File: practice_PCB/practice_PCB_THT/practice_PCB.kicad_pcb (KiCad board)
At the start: 2 copper layers, 97.5 x 96.5 mm, 224 parts, among them J1 5V, J10 GND, J11 5V, J12 GND, J13 5V, J14 GND, J15 5V, J16 GND, J17 5V, J18 GND, J19 5V, J2 GND, J20 GND, J21 5V, J22 GND, J23 5V, J24 GND, J25 5V, J26 GND, J27 5V, J28 GND, J29 5V, J3 5V, J30 GND, J31 5V, J32 GND, J4 GND, J5 5V, J6 GND, J7 5V, J8 GND, J9 5V

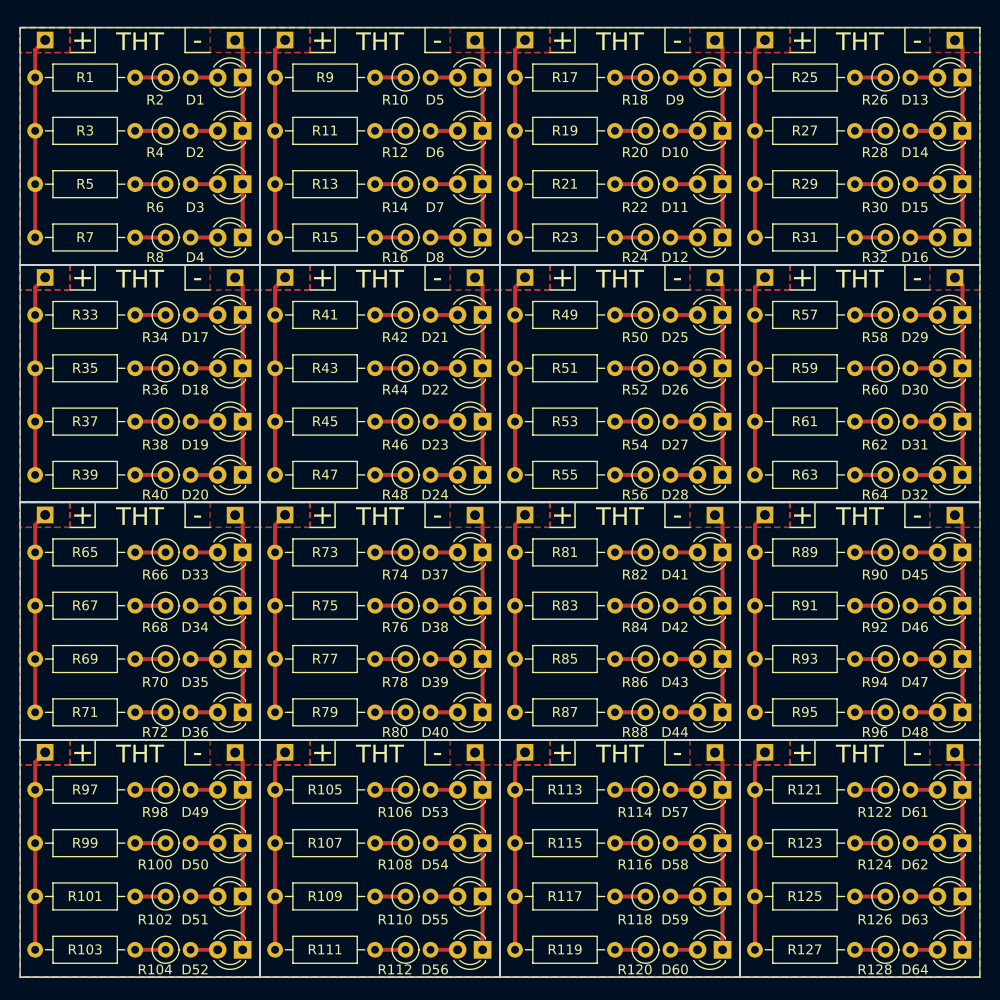
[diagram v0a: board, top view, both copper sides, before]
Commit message: create an array and copy the SMT Array in to the file
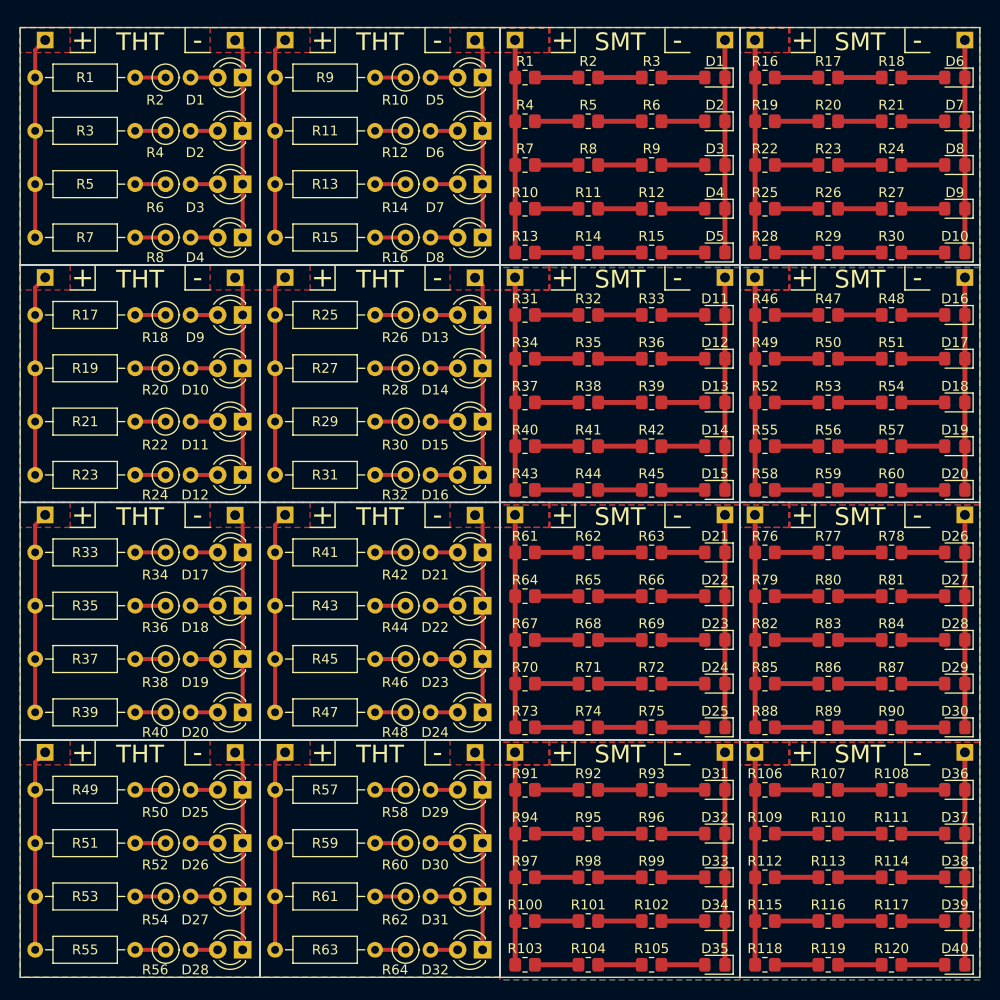
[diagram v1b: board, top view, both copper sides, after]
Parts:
- removed the D10 at (208.5, 76.5)
- removed the D11 at (208.5, 82.0)
- removed the D12 at (208.5, 87.4)
- removed the D13 at (232.9, 71.1)
- removed the D14 at (232.9, 76.5)
- removed the D15 at (232.9, 82.0)
- removed the D16 at (232.9, 87.4)
- removed the D17 at (159.8, 95.2)
- removed the D18 at (159.8, 100.7)
- removed the D19 at (159.8, 106.1)
- removed the D20 at (159.8, 111.5)
- removed the D21 at (184.2, 95.2)
- removed the D22 at (184.2, 100.7)
- removed the D23 at (184.2, 106.1)
- removed the D24 at (184.2, 111.5)
- removed the D25 at (208.5, 95.2)
- removed the D26 at (208.5, 100.7)
- removed the D27 at (208.5, 106.1)
- removed the D28 at (208.5, 111.5)
- removed the D29 at (232.9, 95.2)
- removed the D30 at (232.9, 100.7)
- removed the D31 at (232.9, 106.1)
- removed the D32 at (232.9, 111.5)
- removed D41, D42, D43, D44, D45, D46, D47, D48, D49, D50, D51, D52, D53, D54, D55, D56, D57, D58, D59, D60, D61, D62, D63, D64: LED, LED_THT:LED_D3.0mm
- removed the D9 at (208.5, 71.1)
- removed the J10 at (159.0, 91.5)
- removed the J11 at (164.1, 91.4)
- removed the J12 at (183.4, 91.5)
- removed the J13 at (188.5, 91.4)
- removed the J14 at (207.8, 91.5)
- removed the J15 at (212.9, 91.4)
- removed the J16 at (232.2, 91.5)
- removed J17, J19, J21, J23, J25, J27, J29, J31: 5V, practice_PCB:PinSocket_1x01_P2.54mm_Vertical
- removed J18, J20, J22, J24, J26, J28, J30, J32: GND, practice_PCB:PinSocket_1x01_P2.54mm_Vertical
- removed the J5 at (188.5, 67.3)
- removed the J6 at (207.8, 67.3)
- removed the J7 at (212.9, 67.3)
- removed the J8 at (232.2, 67.3)
- removed the J9 at (139.7, 91.4)
- removed R121, R123, R125, R127: 60, Resistor_THT:R_Axial_DIN0207_L6.3mm_D2.5mm_P10.16mm_Horizontal
- removed R122, R124, R126, R128: 60, Resistor_THT:R_Axial_DIN0207_L6.3mm_D2.5mm_P2.54mm_Vertical
- removed the R17 at (187.5, 71.1)
- removed the R18 at (200.7, 71.1)
- removed the R19 at (187.5, 76.5)
- removed the R20 at (200.7, 76.5)
- removed the R21 at (187.5, 82.0)
- removed the R22 at (200.7, 82.0)
- removed the R23 at (187.5, 87.4)
- removed the R24 at (200.7, 87.4)
- removed the R25 at (211.8, 71.1)
- removed the R26 at (225.1, 71.1)
- removed the R27 at (211.8, 76.5)
- removed the R28 at (225.1, 76.5)
- removed the R29 at (211.8, 82.0)
- removed the R30 at (225.1, 82.0)
- removed the R31 at (211.8, 87.4)
- removed the R32 at (225.1, 87.4)
- removed the R33 at (138.7, 95.2)
- removed the R34 at (151.9, 95.2)
- removed the R35 at (138.7, 100.7)
- removed the R36 at (151.9, 100.7)
- removed the R37 at (138.7, 106.1)
- removed the R38 at (151.9, 106.1)
- removed the R39 at (138.7, 111.5)
- removed the R40 at (151.9, 111.5)
- removed the R41 at (163.1, 95.2)
- removed the R42 at (176.3, 95.2)
- removed the R43 at (163.1, 100.7)
- removed the R44 at (176.3, 100.7)
- removed the R45 at (163.1, 106.1)
- removed the R46 at (176.3, 106.1)
- removed the R47 at (163.1, 111.5)
- removed the R48 at (176.3, 111.5)
- removed the R49 at (187.5, 95.2)
- removed the R50 at (200.7, 95.2)
- removed the R51 at (187.5, 100.7)
- removed the R52 at (200.7, 100.7)
- removed the R53 at (187.5, 106.1)
- removed the R54 at (200.7, 106.1)
- removed the R55 at (187.5, 111.5)
- removed the R56 at (200.7, 111.5)
- removed the R57 at (211.8, 95.2)
- removed the R58 at (225.1, 95.2)
- removed the R59 at (211.8, 100.7)
- removed the R60 at (225.1, 100.7)
- removed the R61 at (211.8, 106.1)
- removed the R62 at (225.1, 106.1)
- removed the R63 at (211.8, 111.5)
- removed the R64 at (225.1, 111.5)
- added D1: LED, LED_SMD:LED_0805_2012Metric_Pad1.15x1.40mm_HandSolder, F.Cu at (207.8, 71.1)
- added D10: LED, LED_SMD:LED_0805_2012Metric_Pad1.15x1.40mm_HandSolder, F.Cu at (232.1, 88.9)
- added D10: LED, LED_THT:LED_D3.0mm, F.Cu at (159.8, 100.7)
- added D11: LED, LED_THT:LED_D3.0mm, F.Cu at (159.8, 106.1)
- added D11: LED, LED_SMD:LED_0805_2012Metric_Pad1.15x1.40mm_HandSolder, F.Cu at (207.8, 95.2)
- added D12: LED, LED_SMD:LED_0805_2012Metric_Pad1.15x1.40mm_HandSolder, F.Cu at (207.8, 99.7)
- added D12: LED, LED_THT:LED_D3.0mm, F.Cu at (159.8, 111.5)
- added D13: LED, LED_THT:LED_D3.0mm, F.Cu at (184.2, 95.2)
- added D13: LED, LED_SMD:LED_0805_2012Metric_Pad1.15x1.40mm_HandSolder, F.Cu at (207.8, 104.1)
- added D14: LED, LED_SMD:LED_0805_2012Metric_Pad1.15x1.40mm_HandSolder, F.Cu at (207.8, 108.6)
- added D14: LED, LED_THT:LED_D3.0mm, F.Cu at (184.2, 100.7)
- added D15: LED, LED_THT:LED_D3.0mm, F.Cu at (184.2, 106.1)
- added D15: LED, LED_SMD:LED_0805_2012Metric_Pad1.15x1.40mm_HandSolder, F.Cu at (207.8, 113.0)
- added D16: LED, LED_THT:LED_D3.0mm, F.Cu at (184.2, 111.5)
- added D16: LED, LED_SMD:LED_0805_2012Metric_Pad1.15x1.40mm_HandSolder, F.Cu at (232.1, 95.2)
- added D17: LED, LED_THT:LED_D3.0mm, F.Cu at (159.8, 119.4)
- added D17: LED, LED_SMD:LED_0805_2012Metric_Pad1.15x1.40mm_HandSolder, F.Cu at (232.1, 99.7)
- added D18: LED, LED_SMD:LED_0805_2012Metric_Pad1.15x1.40mm_HandSolder, F.Cu at (232.1, 104.1)
- added D18: LED, LED_THT:LED_D3.0mm, F.Cu at (159.8, 124.8)
- added D19: LED, LED_THT:LED_D3.0mm, F.Cu at (159.8, 130.2)
- added D19: LED, LED_SMD:LED_0805_2012Metric_Pad1.15x1.40mm_HandSolder, F.Cu at (232.1, 108.6)
- added D2: LED, LED_SMD:LED_0805_2012Metric_Pad1.15x1.40mm_HandSolder, F.Cu at (207.8, 75.6)
- added D20: LED, LED_SMD:LED_0805_2012Metric_Pad1.15x1.40mm_HandSolder, F.Cu at (232.1, 113.0)
- added D20: LED, LED_THT:LED_D3.0mm, F.Cu at (159.8, 135.6)
- added D21: LED, LED_THT:LED_D3.0mm, F.Cu at (184.2, 119.4)
- added D21: LED, LED_SMD:LED_0805_2012Metric_Pad1.15x1.40mm_HandSolder, F.Cu at (207.8, 119.4)
- added D22: LED, LED_THT:LED_D3.0mm, F.Cu at (184.2, 124.8)
- added D22: LED, LED_SMD:LED_0805_2012Metric_Pad1.15x1.40mm_HandSolder, F.Cu at (207.8, 123.8)
- added D23: LED, LED_SMD:LED_0805_2012Metric_Pad1.15x1.40mm_HandSolder, F.Cu at (207.8, 128.3)
- added D23: LED, LED_THT:LED_D3.0mm, F.Cu at (184.2, 130.2)
- added D24: LED, LED_SMD:LED_0805_2012Metric_Pad1.15x1.40mm_HandSolder, F.Cu at (207.8, 132.7)
- added D24: LED, LED_THT:LED_D3.0mm, F.Cu at (184.2, 135.6)
- added D25: LED, LED_SMD:LED_0805_2012Metric_Pad1.15x1.40mm_HandSolder, F.Cu at (207.8, 137.2)
- added D25: LED, LED_THT:LED_D3.0mm, F.Cu at (159.8, 143.5)
- added D26: LED, LED_THT:LED_D3.0mm, F.Cu at (159.8, 148.9)
- added D26: LED, LED_SMD:LED_0805_2012Metric_Pad1.15x1.40mm_HandSolder, F.Cu at (232.1, 119.4)
- added D27: LED, LED_SMD:LED_0805_2012Metric_Pad1.15x1.40mm_HandSolder, F.Cu at (232.1, 123.8)
- added D27: LED, LED_THT:LED_D3.0mm, F.Cu at (159.8, 154.3)
- added D28: LED, LED_SMD:LED_0805_2012Metric_Pad1.15x1.40mm_HandSolder, F.Cu at (232.1, 128.3)
- added D28: LED, LED_THT:LED_D3.0mm, F.Cu at (159.8, 159.8)
- added D29: LED, LED_THT:LED_D3.0mm, F.Cu at (184.2, 143.5)
- added D29: LED, LED_SMD:LED_0805_2012Metric_Pad1.15x1.40mm_HandSolder, F.Cu at (232.1, 132.7)
- added D3: LED, LED_SMD:LED_0805_2012Metric_Pad1.15x1.40mm_HandSolder, F.Cu at (207.8, 80.0)
- added D30: LED, LED_THT:LED_D3.0mm, F.Cu at (184.2, 148.9)
- added D30: LED, LED_SMD:LED_0805_2012Metric_Pad1.15x1.40mm_HandSolder, F.Cu at (232.1, 137.2)
- added D31: LED, LED_SMD:LED_0805_2012Metric_Pad1.15x1.40mm_HandSolder, F.Cu at (207.8, 143.5)
- added D31: LED, LED_THT:LED_D3.0mm, F.Cu at (184.2, 154.3)
- added D32: LED, LED_THT:LED_D3.0mm, F.Cu at (184.2, 159.8)
- added D32: LED, LED_SMD:LED_0805_2012Metric_Pad1.15x1.40mm_HandSolder, F.Cu at (207.8, 148.0)
- added D4: LED, LED_SMD:LED_0805_2012Metric_Pad1.15x1.40mm_HandSolder, F.Cu at (207.8, 84.5)
- added D5: LED, LED_SMD:LED_0805_2012Metric_Pad1.15x1.40mm_HandSolder, F.Cu at (207.8, 88.9)
- added D6: LED, LED_SMD:LED_0805_2012Metric_Pad1.15x1.40mm_HandSolder, F.Cu at (232.1, 71.1)
- added D7: LED, LED_SMD:LED_0805_2012Metric_Pad1.15x1.40mm_HandSolder, F.Cu at (232.1, 75.6)
- added D8: LED, LED_SMD:LED_0805_2012Metric_Pad1.15x1.40mm_HandSolder, F.Cu at (232.1, 80.0)
- added D9: LED, LED_SMD:LED_0805_2012Metric_Pad1.15x1.40mm_HandSolder, F.Cu at (232.1, 84.5)
- added D9: LED, LED_THT:LED_D3.0mm, F.Cu at (159.8, 95.2)
- added G***: LOGO, practice_PCB:MWG, B.Cu at (205.7, 86.4)
- added G***1: LOGO, practice_PCB:MWG, B.Cu at (230.1, 86.4)
- added G***2: LOGO, practice_PCB:MWG, B.Cu at (205.7, 110.5)
- added G***3: LOGO, practice_PCB:MWG, B.Cu at (230.1, 110.5)
- added G***4: LOGO, practice_PCB:MWG, B.Cu at (205.7, 134.6)
- added G***5: LOGO, practice_PCB:MWG, B.Cu at (230.1, 134.6)
- added G***6: LOGO, practice_PCB:MWG, B.Cu at (205.7, 158.8)
- added G***7: LOGO, practice_PCB:MWG, B.Cu at (230.1, 158.8)
- added J1: 5V, practice_PCB:PinSocket_1x01_P2.54mm_Vertical, F.Cu at (187.5, 67.3)
- added J10: GND, practice_PCB:PinSocket_1x01_P2.54mm_Vertical, F.Cu at (159.0, 115.6)
- added J10: GND, practice_PCB:PinSocket_1x01_P2.54mm_Vertical, F.Cu at (208.8, 115.6)
- added J11: 5V, practice_PCB:PinSocket_1x01_P2.54mm_Vertical, F.Cu at (164.1, 115.6)
- added J11: 5V, practice_PCB:PinSocket_1x01_P2.54mm_Vertical, F.Cu at (211.8, 115.6)
- added J12: GND, practice_PCB:PinSocket_1x01_P2.54mm_Vertical, F.Cu at (183.4, 115.6)
- added J12: GND, practice_PCB:PinSocket_1x01_P2.54mm_Vertical, F.Cu at (233.2, 115.6)
- added J13: 5V, practice_PCB:PinSocket_1x01_P2.54mm_Vertical, F.Cu at (139.7, 139.7)
- added J13: 5V, practice_PCB:PinSocket_1x01_P2.54mm_Vertical, F.Cu at (187.5, 139.7)
- added J14: GND, practice_PCB:PinSocket_1x01_P2.54mm_Vertical, F.Cu at (159.0, 139.7)
- added J14: GND, practice_PCB:PinSocket_1x01_P2.54mm_Vertical, F.Cu at (208.8, 139.7)
- added J15: 5V, practice_PCB:PinSocket_1x01_P2.54mm_Vertical, F.Cu at (164.1, 139.7)
- added J15: 5V, practice_PCB:PinSocket_1x01_P2.54mm_Vertical, F.Cu at (211.8, 139.7)
- added J16: GND, practice_PCB:PinSocket_1x01_P2.54mm_Vertical, F.Cu at (233.2, 139.7)
- added J16: GND, practice_PCB:PinSocket_1x01_P2.54mm_Vertical, F.Cu at (183.4, 139.7)
- added J2: GND, practice_PCB:PinSocket_1x01_P2.54mm_Vertical, F.Cu at (208.8, 67.3)
- added J3: 5V, practice_PCB:PinSocket_1x01_P2.54mm_Vertical, F.Cu at (211.8, 67.3)
- added J4: GND, practice_PCB:PinSocket_1x01_P2.54mm_Vertical, F.Cu at (233.2, 67.3)
- added J5: 5V, practice_PCB:PinSocket_1x01_P2.54mm_Vertical, F.Cu at (139.7, 91.4)
- added J5: 5V, practice_PCB:PinSocket_1x01_P2.54mm_Vertical, F.Cu at (187.5, 91.4)
- added J6: GND, practice_PCB:PinSocket_1x01_P2.54mm_Vertical, F.Cu at (159.0, 91.5)
- added J6: GND, practice_PCB:PinSocket_1x01_P2.54mm_Vertical, F.Cu at (208.8, 91.4)
- added J7: 5V, practice_PCB:PinSocket_1x01_P2.54mm_Vertical, F.Cu at (211.8, 91.4)
- added J7: 5V, practice_PCB:PinSocket_1x01_P2.54mm_Vertical, F.Cu at (164.1, 91.4)
- added J8: GND, practice_PCB:PinSocket_1x01_P2.54mm_Vertical, F.Cu at (233.2, 91.4)
- added J8: GND, practice_PCB:PinSocket_1x01_P2.54mm_Vertical, F.Cu at (183.4, 91.5)
- added J9: 5V, practice_PCB:PinSocket_1x01_P2.54mm_Vertical, F.Cu at (139.7, 115.6)
- added J9: 5V, practice_PCB:PinSocket_1x01_P2.54mm_Vertical, F.Cu at (187.5, 115.6)
- added R1: 60, Resistor_SMD:R_0805_2012Metric_Pad1.20x1.40mm_HandSolder, F.Cu at (188.5, 71.1)
- added R10: 60, Resistor_SMD:R_0805_2012Metric_Pad1.20x1.40mm_HandSolder, F.Cu at (188.5, 84.5)
- added R11: 60, Resistor_SMD:R_0805_2012Metric_Pad1.20x1.40mm_HandSolder, F.Cu at (194.9, 84.5)
- added R12: 60, Resistor_SMD:R_0805_2012Metric_Pad1.20x1.40mm_HandSolder, F.Cu at (201.3, 84.5)
- added R13: 60, Resistor_SMD:R_0805_2012Metric_Pad1.20x1.40mm_HandSolder, F.Cu at (188.5, 88.9)
- added R14: 60, Resistor_SMD:R_0805_2012Metric_Pad1.20x1.40mm_HandSolder, F.Cu at (194.9, 88.9)
- added R15: 60, Resistor_SMD:R_0805_2012Metric_Pad1.20x1.40mm_HandSolder, F.Cu at (201.3, 88.9)
- added R16: 60, Resistor_SMD:R_0805_2012Metric_Pad1.20x1.40mm_HandSolder, F.Cu at (212.9, 71.1)
- added R17: 60, Resistor_SMD:R_0805_2012Metric_Pad1.20x1.40mm_HandSolder, F.Cu at (219.3, 71.1)
- added R17: 60, Resistor_THT:R_Axial_DIN0207_L6.3mm_D2.5mm_P10.16mm_Horizontal, F.Cu at (138.7, 95.2)
- added R18: 60, Resistor_THT:R_Axial_DIN0207_L6.3mm_D2.5mm_P2.54mm_Vertical, F.Cu at (151.9, 95.2)
- added R18: 60, Resistor_SMD:R_0805_2012Metric_Pad1.20x1.40mm_HandSolder, F.Cu at (225.7, 71.1)
- added R19: 60, Resistor_THT:R_Axial_DIN0207_L6.3mm_D2.5mm_P10.16mm_Horizontal, F.Cu at (138.7, 100.7)
- added R19: 60, Resistor_SMD:R_0805_2012Metric_Pad1.20x1.40mm_HandSolder, F.Cu at (212.9, 75.6)
- added R2: 60, Resistor_SMD:R_0805_2012Metric_Pad1.20x1.40mm_HandSolder, F.Cu at (194.9, 71.1)
- added R20: 60, Resistor_SMD:R_0805_2012Metric_Pad1.20x1.40mm_HandSolder, F.Cu at (219.3, 75.6)
- added R20: 60, Resistor_THT:R_Axial_DIN0207_L6.3mm_D2.5mm_P2.54mm_Vertical, F.Cu at (151.9, 100.7)
- added R21: 60, Resistor_THT:R_Axial_DIN0207_L6.3mm_D2.5mm_P10.16mm_Horizontal, F.Cu at (138.7, 106.1)
- added R21: 60, Resistor_SMD:R_0805_2012Metric_Pad1.20x1.40mm_HandSolder, F.Cu at (225.7, 75.6)
- added R22: 60, Resistor_THT:R_Axial_DIN0207_L6.3mm_D2.5mm_P2.54mm_Vertical, F.Cu at (151.9, 106.1)
- added R22: 60, Resistor_SMD:R_0805_2012Metric_Pad1.20x1.40mm_HandSolder, F.Cu at (212.9, 80.0)
- added R23: 60, Resistor_SMD:R_0805_2012Metric_Pad1.20x1.40mm_HandSolder, F.Cu at (219.3, 80.0)
- added R23: 60, Resistor_THT:R_Axial_DIN0207_L6.3mm_D2.5mm_P10.16mm_Horizontal, F.Cu at (138.7, 111.5)
- added R24: 60, Resistor_SMD:R_0805_2012Metric_Pad1.20x1.40mm_HandSolder, F.Cu at (225.7, 80.0)
- added R24: 60, Resistor_THT:R_Axial_DIN0207_L6.3mm_D2.5mm_P2.54mm_Vertical, F.Cu at (151.9, 111.5)
- added R25: 60, Resistor_THT:R_Axial_DIN0207_L6.3mm_D2.5mm_P10.16mm_Horizontal, F.Cu at (163.1, 95.2)
- added R25: 60, Resistor_SMD:R_0805_2012Metric_Pad1.20x1.40mm_HandSolder, F.Cu at (212.9, 84.5)
- added R26: 60, Resistor_THT:R_Axial_DIN0207_L6.3mm_D2.5mm_P2.54mm_Vertical, F.Cu at (176.3, 95.2)
- added R26: 60, Resistor_SMD:R_0805_2012Metric_Pad1.20x1.40mm_HandSolder, F.Cu at (219.3, 84.5)
- added R27: 60, Resistor_SMD:R_0805_2012Metric_Pad1.20x1.40mm_HandSolder, F.Cu at (225.7, 84.5)
- added R27: 60, Resistor_THT:R_Axial_DIN0207_L6.3mm_D2.5mm_P10.16mm_Horizontal, F.Cu at (163.1, 100.7)
- added R28: 60, Resistor_THT:R_Axial_DIN0207_L6.3mm_D2.5mm_P2.54mm_Vertical, F.Cu at (176.3, 100.7)
- added R28: 60, Resistor_SMD:R_0805_2012Metric_Pad1.20x1.40mm_HandSolder, F.Cu at (212.9, 88.9)
- added R29: 60, Resistor_THT:R_Axial_DIN0207_L6.3mm_D2.5mm_P10.16mm_Horizontal, F.Cu at (163.1, 106.1)
- added R29: 60, Resistor_SMD:R_0805_2012Metric_Pad1.20x1.40mm_HandSolder, F.Cu at (219.3, 88.9)
- added R3: 60, Resistor_SMD:R_0805_2012Metric_Pad1.20x1.40mm_HandSolder, F.Cu at (201.3, 71.1)
- added R30: 60, Resistor_SMD:R_0805_2012Metric_Pad1.20x1.40mm_HandSolder, F.Cu at (225.7, 88.9)
- added R30: 60, Resistor_THT:R_Axial_DIN0207_L6.3mm_D2.5mm_P2.54mm_Vertical, F.Cu at (176.3, 106.1)
- added R31: 60, Resistor_SMD:R_0805_2012Metric_Pad1.20x1.40mm_HandSolder, F.Cu at (188.5, 95.2)
- added R31: 60, Resistor_THT:R_Axial_DIN0207_L6.3mm_D2.5mm_P10.16mm_Horizontal, F.Cu at (163.1, 111.5)
- added R32: 60, Resistor_THT:R_Axial_DIN0207_L6.3mm_D2.5mm_P2.54mm_Vertical, F.Cu at (176.3, 111.5)
- added R32: 60, Resistor_SMD:R_0805_2012Metric_Pad1.20x1.40mm_HandSolder, F.Cu at (194.9, 95.2)
- added R33: 60, Resistor_THT:R_Axial_DIN0207_L6.3mm_D2.5mm_P10.16mm_Horizontal, F.Cu at (138.7, 119.4)
- added R33: 60, Resistor_SMD:R_0805_2012Metric_Pad1.20x1.40mm_HandSolder, F.Cu at (201.3, 95.2)
- added R34: 60, Resistor_SMD:R_0805_2012Metric_Pad1.20x1.40mm_HandSolder, F.Cu at (188.5, 99.7)
- added R34: 60, Resistor_THT:R_Axial_DIN0207_L6.3mm_D2.5mm_P2.54mm_Vertical, F.Cu at (151.9, 119.4)
- added R35: 60, Resistor_SMD:R_0805_2012Metric_Pad1.20x1.40mm_HandSolder, F.Cu at (194.9, 99.7)
- added R35: 60, Resistor_THT:R_Axial_DIN0207_L6.3mm_D2.5mm_P10.16mm_Horizontal, F.Cu at (138.7, 124.8)
- added R36: 60, Resistor_THT:R_Axial_DIN0207_L6.3mm_D2.5mm_P2.54mm_Vertical, F.Cu at (151.9, 124.8)
- added R36: 60, Resistor_SMD:R_0805_2012Metric_Pad1.20x1.40mm_HandSolder, F.Cu at (201.3, 99.7)
- added R37: 60, Resistor_SMD:R_0805_2012Metric_Pad1.20x1.40mm_HandSolder, F.Cu at (188.5, 104.1)
- added R37: 60, Resistor_THT:R_Axial_DIN0207_L6.3mm_D2.5mm_P10.16mm_Horizontal, F.Cu at (138.7, 130.2)
- added R38: 60, Resistor_THT:R_Axial_DIN0207_L6.3mm_D2.5mm_P2.54mm_Vertical, F.Cu at (151.9, 130.2)
- added R38: 60, Resistor_SMD:R_0805_2012Metric_Pad1.20x1.40mm_HandSolder, F.Cu at (194.9, 104.1)
- added R39: 60, Resistor_THT:R_Axial_DIN0207_L6.3mm_D2.5mm_P10.16mm_Horizontal, F.Cu at (138.7, 135.6)
- added R39: 60, Resistor_SMD:R_0805_2012Metric_Pad1.20x1.40mm_HandSolder, F.Cu at (201.3, 104.1)
- added R4: 60, Resistor_SMD:R_0805_2012Metric_Pad1.20x1.40mm_HandSolder, F.Cu at (188.5, 75.6)
- added R40: 60, Resistor_THT:R_Axial_DIN0207_L6.3mm_D2.5mm_P2.54mm_Vertical, F.Cu at (151.9, 135.6)
- added R40: 60, Resistor_SMD:R_0805_2012Metric_Pad1.20x1.40mm_HandSolder, F.Cu at (188.5, 108.6)
- added R41: 60, Resistor_SMD:R_0805_2012Metric_Pad1.20x1.40mm_HandSolder, F.Cu at (194.9, 108.6)
- added R41: 60, Resistor_THT:R_Axial_DIN0207_L6.3mm_D2.5mm_P10.16mm_Horizontal, F.Cu at (163.1, 119.4)
- added R42: 60, Resistor_THT:R_Axial_DIN0207_L6.3mm_D2.5mm_P2.54mm_Vertical, F.Cu at (176.3, 119.4)
- added R42: 60, Resistor_SMD:R_0805_2012Metric_Pad1.20x1.40mm_HandSolder, F.Cu at (201.3, 108.6)
- added R43: 60, Resistor_THT:R_Axial_DIN0207_L6.3mm_D2.5mm_P10.16mm_Horizontal, F.Cu at (163.1, 124.8)
- added R43: 60, Resistor_SMD:R_0805_2012Metric_Pad1.20x1.40mm_HandSolder, F.Cu at (188.5, 113.0)
- added R44: 60, Resistor_THT:R_Axial_DIN0207_L6.3mm_D2.5mm_P2.54mm_Vertical, F.Cu at (176.3, 124.8)
- added R44: 60, Resistor_SMD:R_0805_2012Metric_Pad1.20x1.40mm_HandSolder, F.Cu at (194.9, 113.0)
- added R45: 60, Resistor_SMD:R_0805_2012Metric_Pad1.20x1.40mm_HandSolder, F.Cu at (201.3, 113.0)
- added R45: 60, Resistor_THT:R_Axial_DIN0207_L6.3mm_D2.5mm_P10.16mm_Horizontal, F.Cu at (163.1, 130.2)
- added R46: 60, Resistor_THT:R_Axial_DIN0207_L6.3mm_D2.5mm_P2.54mm_Vertical, F.Cu at (176.3, 130.2)
- added R46: 60, Resistor_SMD:R_0805_2012Metric_Pad1.20x1.40mm_HandSolder, F.Cu at (212.9, 95.2)
- added R47: 60, Resistor_SMD:R_0805_2012Metric_Pad1.20x1.40mm_HandSolder, F.Cu at (219.3, 95.2)
- added R47: 60, Resistor_THT:R_Axial_DIN0207_L6.3mm_D2.5mm_P10.16mm_Horizontal, F.Cu at (163.1, 135.6)
- added R48: 60, Resistor_SMD:R_0805_2012Metric_Pad1.20x1.40mm_HandSolder, F.Cu at (225.7, 95.2)
- added R48: 60, Resistor_THT:R_Axial_DIN0207_L6.3mm_D2.5mm_P2.54mm_Vertical, F.Cu at (176.3, 135.6)
- added R49: 60, Resistor_SMD:R_0805_2012Metric_Pad1.20x1.40mm_HandSolder, F.Cu at (212.9, 99.7)
- added R49: 60, Resistor_THT:R_Axial_DIN0207_L6.3mm_D2.5mm_P10.16mm_Horizontal, F.Cu at (138.7, 143.5)
- added R5: 60, Resistor_SMD:R_0805_2012Metric_Pad1.20x1.40mm_HandSolder, F.Cu at (194.9, 75.6)
- added R50: 60, Resistor_SMD:R_0805_2012Metric_Pad1.20x1.40mm_HandSolder, F.Cu at (219.3, 99.7)
- added R50: 60, Resistor_THT:R_Axial_DIN0207_L6.3mm_D2.5mm_P2.54mm_Vertical, F.Cu at (151.9, 143.5)
- added R51: 60, Resistor_SMD:R_0805_2012Metric_Pad1.20x1.40mm_HandSolder, F.Cu at (225.7, 99.7)
- added R51: 60, Resistor_THT:R_Axial_DIN0207_L6.3mm_D2.5mm_P10.16mm_Horizontal, F.Cu at (138.7, 148.9)
- added R52: 60, Resistor_THT:R_Axial_DIN0207_L6.3mm_D2.5mm_P2.54mm_Vertical, F.Cu at (151.9, 148.9)
- added R52: 60, Resistor_SMD:R_0805_2012Metric_Pad1.20x1.40mm_HandSolder, F.Cu at (212.9, 104.1)
- added R53: 60, Resistor_THT:R_Axial_DIN0207_L6.3mm_D2.5mm_P10.16mm_Horizontal, F.Cu at (138.7, 154.3)
- added R53: 60, Resistor_SMD:R_0805_2012Metric_Pad1.20x1.40mm_HandSolder, F.Cu at (219.3, 104.1)
- added R54: 60, Resistor_SMD:R_0805_2012Metric_Pad1.20x1.40mm_HandSolder, F.Cu at (225.7, 104.1)
- added R54: 60, Resistor_THT:R_Axial_DIN0207_L6.3mm_D2.5mm_P2.54mm_Vertical, F.Cu at (151.9, 154.3)
- added R55: 60, Resistor_THT:R_Axial_DIN0207_L6.3mm_D2.5mm_P10.16mm_Horizontal, F.Cu at (138.7, 159.8)
- added R55: 60, Resistor_SMD:R_0805_2012Metric_Pad1.20x1.40mm_HandSolder, F.Cu at (212.9, 108.6)
- added R56: 60, Resistor_SMD:R_0805_2012Metric_Pad1.20x1.40mm_HandSolder, F.Cu at (219.3, 108.6)
- added R56: 60, Resistor_THT:R_Axial_DIN0207_L6.3mm_D2.5mm_P2.54mm_Vertical, F.Cu at (151.9, 159.8)
- added R57: 60, Resistor_THT:R_Axial_DIN0207_L6.3mm_D2.5mm_P10.16mm_Horizontal, F.Cu at (163.1, 143.5)
- added R57: 60, Resistor_SMD:R_0805_2012Metric_Pad1.20x1.40mm_HandSolder, F.Cu at (225.7, 108.6)
- added R58: 60, Resistor_THT:R_Axial_DIN0207_L6.3mm_D2.5mm_P2.54mm_Vertical, F.Cu at (176.3, 143.5)
- added R58: 60, Resistor_SMD:R_0805_2012Metric_Pad1.20x1.40mm_HandSolder, F.Cu at (212.9, 113.0)
- added R59: 60, Resistor_SMD:R_0805_2012Metric_Pad1.20x1.40mm_HandSolder, F.Cu at (219.3, 113.0)
- added R59: 60, Resistor_THT:R_Axial_DIN0207_L6.3mm_D2.5mm_P10.16mm_Horizontal, F.Cu at (163.1, 148.9)
- added R6: 60, Resistor_SMD:R_0805_2012Metric_Pad1.20x1.40mm_HandSolder, F.Cu at (201.3, 75.6)
- added R60: 60, Resistor_SMD:R_0805_2012Metric_Pad1.20x1.40mm_HandSolder, F.Cu at (225.7, 113.0)
- added R60: 60, Resistor_THT:R_Axial_DIN0207_L6.3mm_D2.5mm_P2.54mm_Vertical, F.Cu at (176.3, 148.9)
- added R61: 60, Resistor_SMD:R_0805_2012Metric_Pad1.20x1.40mm_HandSolder, F.Cu at (188.5, 119.4)
- added R61: 60, Resistor_THT:R_Axial_DIN0207_L6.3mm_D2.5mm_P10.16mm_Horizontal, F.Cu at (163.1, 154.3)
- added R62: 60, Resistor_SMD:R_0805_2012Metric_Pad1.20x1.40mm_HandSolder, F.Cu at (194.9, 119.4)
- added R62: 60, Resistor_THT:R_Axial_DIN0207_L6.3mm_D2.5mm_P2.54mm_Vertical, F.Cu at (176.3, 154.3)
- added R63: 60, Resistor_SMD:R_0805_2012Metric_Pad1.20x1.40mm_HandSolder, F.Cu at (201.3, 119.4)
- added R63: 60, Resistor_THT:R_Axial_DIN0207_L6.3mm_D2.5mm_P10.16mm_Horizontal, F.Cu at (163.1, 159.8)
- added R64: 60, Resistor_SMD:R_0805_2012Metric_Pad1.20x1.40mm_HandSolder, F.Cu at (188.5, 123.8)
- added R64: 60, Resistor_THT:R_Axial_DIN0207_L6.3mm_D2.5mm_P2.54mm_Vertical, F.Cu at (176.3, 159.8)
- added R7: 60, Resistor_SMD:R_0805_2012Metric_Pad1.20x1.40mm_HandSolder, F.Cu at (188.5, 80.0)
- added R8: 60, Resistor_SMD:R_0805_2012Metric_Pad1.20x1.40mm_HandSolder, F.Cu at (194.9, 80.0)
- added R9: 60, Resistor_SMD:R_0805_2012Metric_Pad1.20x1.40mm_HandSolder, F.Cu at (201.3, 80.0)
- D33, D34, D35, D36, D37, D38, D39, D40: footprint LED_THT:LED_D3.0mm -> LED_SMD:LED_0805_2012Metric_Pad1.15x1.40mm_HandSolder
- R100, R102, R104, R106, R108, R110, R112, R114, R116, R118, R120, R66, R68, R70, R72, R74, R76, R78, R80, R82, R84, R86, R88, R90, R92, R94, R96, R98: footprint Resistor_THT:R_Axial_DIN0207_L6.3mm_D2.5mm_P2.54mm_Vertical -> Resistor_SMD:R_0805_2012Metric_Pad1.20x1.40mm_HandSolder
- R101, R103, R105, R107, R109, R111, R113, R115, R117, R119, R65, R67, R69, R71, R73, R75, R77, R79, R81, R83, R85, R87, R89, R91, R93, R95, R97, R99: footprint Resistor_THT:R_Axial_DIN0207_L6.3mm_D2.5mm_P10.16mm_Horizontal -> Resistor_SMD:R_0805_2012Metric_Pad1.20x1.40mm_HandSolder
- moved D36 72.8 mm to (232.1, 143.5)
- moved R111 63.8 mm to (225.7, 148.0)
- moved R99 62.7 mm to (201.3, 152.4)
- moved R69 62.7 mm to (201.3, 128.3)
- moved D33 58.3 mm to (207.8, 152.4)
- moved D34 57.7 mm to (207.8, 156.8)
- moved R77 57.3 mm to (219.3, 119.4)
- moved D35 57.2 mm to (207.8, 161.3)
- moved R107 56.5 mm to (219.3, 143.5)
- moved R65 56.4 mm to (194.9, 123.8)
- moved R71 56.3 mm to (194.9, 132.7)
- moved R101 56.3 mm to (194.9, 156.8)
- moved D37 55.9 mm to (232.1, 148.0)
- moved D38 55.4 mm to (232.1, 152.4)
- moved D39 54.9 mm to (232.1, 156.8)
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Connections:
- D33 pad 2: Net-(D1-Pad2) -> Net-(D3-Pad2)
- D34 pad 2: Net-(D2-Pad2) -> Net-(D4-Pad2)
- D35 pad 2: Net-(D3-Pad2) -> (no net)
- D36 pad 2: Net-(D4-Pad2) -> Net-(D1-Pad2)
- D37 pad 2: Net-(D1-Pad2) -> Net-(D2-Pad2)
- D38 pad 2: Net-(D2-Pad2) -> Net-(D3-Pad2)
- D39 pad 2: Net-(D3-Pad2) -> Net-(D4-Pad2)
- D40 pad 2: Net-(D4-Pad2) -> (no net)
- R100 pad 1: Net-(R3-Pad2) -> +5V
- R100 pad 2: Net-(D2-Pad2) -> (no net)
- R101 pad 1: +5V -> (no net)
- R101 pad 2: Net-(R5-Pad2) -> (no net)
- R102 pad 1: Net-(R5-Pad2) -> (no net)
- R102 pad 2: Net-(D3-Pad2) -> Net-(D4-Pad2)
- R103 pad 2: Net-(R7-Pad2) -> (no net)
- R104 pad 1: Net-(R7-Pad2) -> (no net)
- R104 pad 2: Net-(D4-Pad2) -> (no net)
- R105 pad 1: +5V -> (no net)
- R105 pad 2: Net-(R1-Pad2) -> (no net)
- R106 pad 1: Net-(R1-Pad2) -> +5V
- R106 pad 2: Net-(D1-Pad2) -> Net-(R1-Pad2)
- R107 pad 1: +5V -> Net-(R1-Pad2)
- R107 pad 2: Net-(R3-Pad2) -> (no net)
- R108 pad 1: Net-(R3-Pad2) -> (no net)
- R108 pad 2: Net-(D2-Pad2) -> Net-(D1-Pad2)
- R109 pad 2: Net-(R5-Pad2) -> (no net)
- R110 pad 1: Net-(R5-Pad2) -> (no net)
- R110 pad 2: Net-(D3-Pad2) -> Net-(R5-Pad2)
- R111 pad 1: +5V -> Net-(R5-Pad2)
- R111 pad 2: Net-(R7-Pad2) -> Net-(D2-Pad2)
- R112 pad 1: Net-(R7-Pad2) -> +5V
- R112 pad 2: Net-(D4-Pad2) -> Net-(R7-Pad2)
- R113 pad 1: +5V -> Net-(R7-Pad2)
- R113 pad 2: Net-(R1-Pad2) -> (no net)
- R114 pad 1: Net-(R1-Pad2) -> (no net)
- R114 pad 2: Net-(D1-Pad2) -> Net-(D3-Pad2)
- R115 pad 2: Net-(R3-Pad2) -> (no net)
- R116 pad 1: Net-(R3-Pad2) -> (no net)
- R116 pad 2: Net-(D2-Pad2) -> (no net)
- R117 pad 1: +5V -> (no net)
- R117 pad 2: Net-(R5-Pad2) -> Net-(D4-Pad2)
- R118 pad 1: Net-(R5-Pad2) -> +5V
- R118 pad 2: Net-(D3-Pad2) -> (no net)
- R119 pad 1: +5V -> (no net)
- R119 pad 2: Net-(R7-Pad2) -> (no net)
- R120 pad 1: Net-(R7-Pad2) -> (no net)
- R120 pad 2: Net-(D4-Pad2) -> (no net)
- R65 pad 1: +5V -> (no net)
- R65 pad 2: Net-(R1-Pad2) -> Net-(R5-Pad2)
- R66 pad 1: Net-(R1-Pad2) -> Net-(R5-Pad2)
- R66 pad 2: Net-(D1-Pad2) -> Net-(D2-Pad2)
- R67 pad 2: Net-(R3-Pad2) -> Net-(R7-Pad2)
- R68 pad 1: Net-(R3-Pad2) -> Net-(R7-Pad2)
- R68 pad 2: Net-(D2-Pad2) -> (no net)
- R69 pad 1: +5V -> (no net)
- R69 pad 2: Net-(R5-Pad2) -> Net-(D3-Pad2)
- R70 pad 1: Net-(R5-Pad2) -> +5V
- R70 pad 2: Net-(D3-Pad2) -> (no net)
- R71 pad 1: +5V -> (no net)
- R71 pad 2: Net-(R7-Pad2) -> (no net)
- R72 pad 1: Net-(R7-Pad2) -> (no net)
- R73 pad 2: Net-(R1-Pad2) -> (no net)
- R74 pad 1: Net-(R1-Pad2) -> (no net)
- R74 pad 2: Net-(D1-Pad2) -> (no net)
- R75 pad 1: +5V -> (no net)
- R75 pad 2: Net-(R3-Pad2) -> (no net)
- R76 pad 1: Net-(R3-Pad2) -> +5V
- R76 pad 2: Net-(D2-Pad2) -> Net-(R1-Pad2)
- R77 pad 1: +5V -> Net-(R1-Pad2)
- R77 pad 2: Net-(R5-Pad2) -> (no net)
- R78 pad 1: Net-(R5-Pad2) -> (no net)
- R78 pad 2: Net-(D3-Pad2) -> Net-(D1-Pad2)
- R79 pad 2: Net-(R7-Pad2) -> (no net)
- R80 pad 1: Net-(R7-Pad2) -> (no net)
- R80 pad 2: Net-(D4-Pad2) -> Net-(R5-Pad2)
- R81 pad 1: +5V -> Net-(R5-Pad2)
- R81 pad 2: Net-(R1-Pad2) -> Net-(D2-Pad2)
- R82 pad 1: Net-(R1-Pad2) -> +5V
- R82 pad 2: Net-(D1-Pad2) -> Net-(R7-Pad2)
- R83 pad 1: +5V -> Net-(R7-Pad2)
- R83 pad 2: Net-(R3-Pad2) -> (no net)
- R84 pad 1: Net-(R3-Pad2) -> (no net)
- R84 pad 2: Net-(D2-Pad2) -> Net-(D3-Pad2)
- R85 pad 2: Net-(R5-Pad2) -> (no net)
- R86 pad 1: Net-(R5-Pad2) -> (no net)
- R86 pad 2: Net-(D3-Pad2) -> (no net)
- R87 pad 1: +5V -> (no net)
- R87 pad 2: Net-(R7-Pad2) -> Net-(D4-Pad2)
- R88 pad 1: Net-(R7-Pad2) -> +5V
- R88 pad 2: Net-(D4-Pad2) -> (no net)
- R89 pad 1: +5V -> (no net)
- R89 pad 2: Net-(R1-Pad2) -> (no net)
- R90 pad 1: Net-(R1-Pad2) -> (no net)
- R90 pad 2: Net-(D1-Pad2) -> (no net)
- R91 pad 2: Net-(R3-Pad2) -> Net-(R1-Pad2)
- R92 pad 1: Net-(R3-Pad2) -> Net-(R1-Pad2)
- R92 pad 2: Net-(D2-Pad2) -> (no net)
- R93 pad 1: +5V -> (no net)
- R93 pad 2: Net-(R5-Pad2) -> Net-(D1-Pad2)
- R94 pad 1: Net-(R5-Pad2) -> +5V
- R94 pad 2: Net-(D3-Pad2) -> (no net)
- R95 pad 1: +5V -> (no net)
- R95 pad 2: Net-(R7-Pad2) -> Net-(R5-Pad2)
- R96 pad 1: Net-(R7-Pad2) -> Net-(R5-Pad2)
- R96 pad 2: Net-(D4-Pad2) -> Net-(D2-Pad2)
- R97 pad 2: Net-(R1-Pad2) -> Net-(R7-Pad2)
- R98 pad 1: Net-(R1-Pad2) -> Net-(R7-Pad2)
- R98 pad 2: Net-(D1-Pad2) -> (no net)
- R99 pad 1: +5V -> (no net)
- R99 pad 2: Net-(R3-Pad2) -> Net-(D3-Pad2)
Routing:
- net (no net): track 0.00 -> 283.4 mm
- net Net-(R3-Pad2): track 49.5 -> 24.7 mm
- net Net-(D4-Pad2): track 44.1 -> 57.3 mm
- net Net-(D3-Pad2): track 44.1 -> 57.3 mm
- net Net-(D2-Pad2): track 44.1 -> 57.3 mm
- net Net-(D1-Pad2): track 44.1 -> 57.3 mm
- net Net-(R7-Pad2): track 49.5 -> 60.2 mm
- net Net-(R1-Pad2): track 49.5 -> 60.2 mm
- net Net-(R5-Pad2): track 49.5 -> 60.2 mm
- net GND: track 325.7 -> 335.6 mm
- net +5V: track 327.8 -> 336.7 mm
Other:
- board text added: "5x LED 15x Widerstand"
- board text added: "SMT"
- board text added: "Unterstützt durch"
- board text added: "zum SMT Löten Bauteilgröße 0805"
